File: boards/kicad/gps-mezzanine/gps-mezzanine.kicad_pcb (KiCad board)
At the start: 2 copper layers, 55 x 54 mm, 17 parts, among them J1 CONN_01X04, P1 CONN_02X20, U1 MCP1700T-3302E/TT, U2 FGPMMOPA6H, U3 TXS0104E

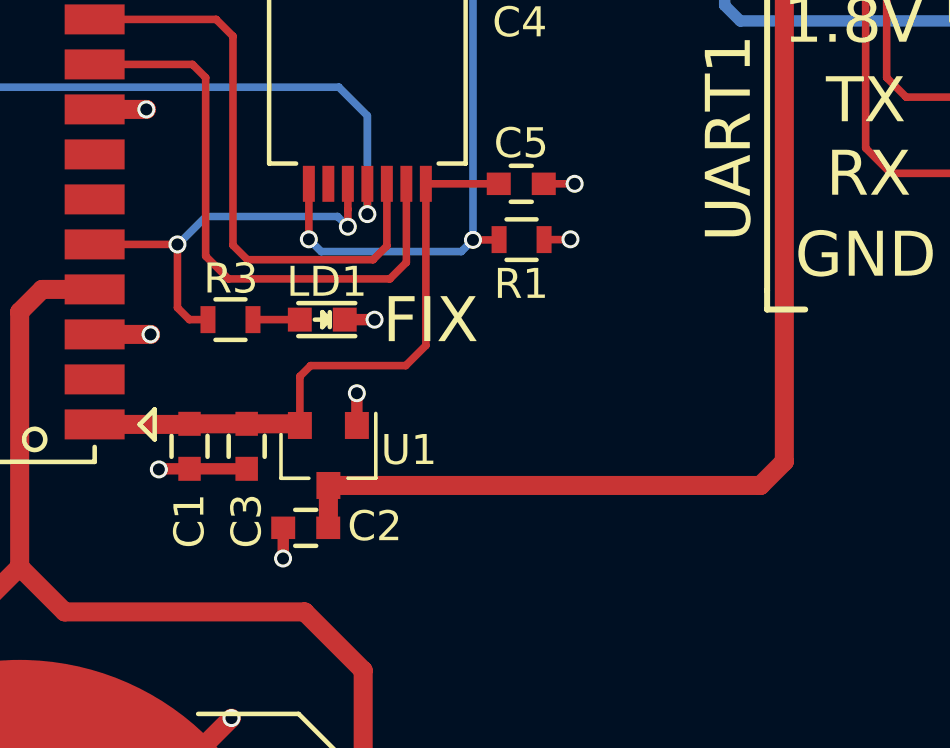
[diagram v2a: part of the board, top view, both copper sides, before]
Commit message: Add ferrite bead to GPS power supply
Signed-off-by: Michael Welling <mwelling@ieee.org>
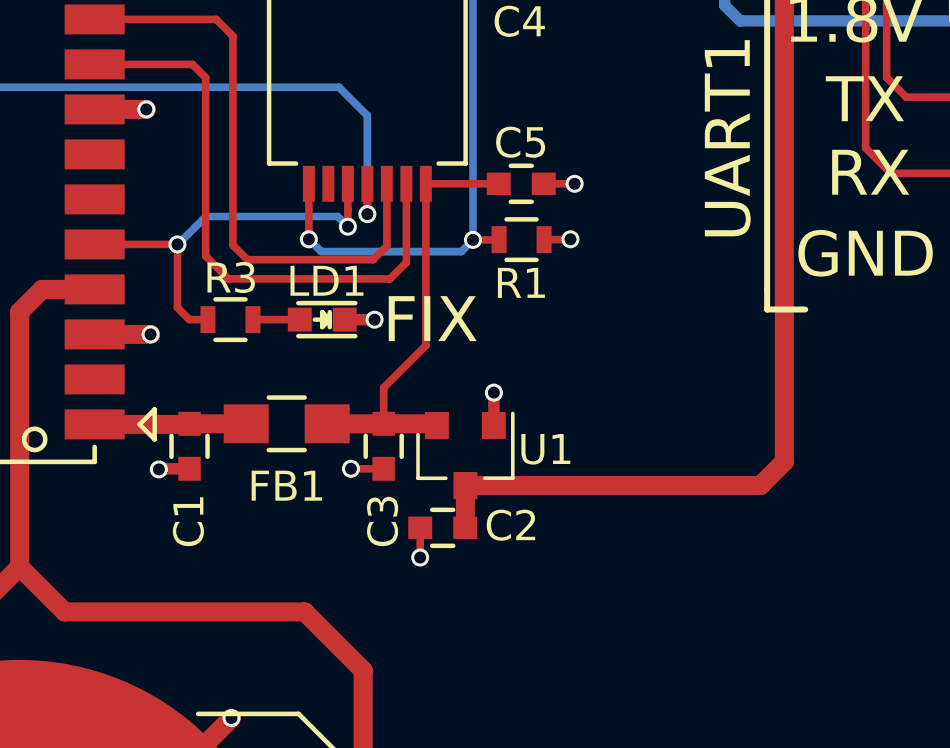
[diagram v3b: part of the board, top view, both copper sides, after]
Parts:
- added FB1: ILBB0805ER102V, Resistors_SMD:R_0805_HandSoldering, F.Cu at (129.4, 125.7)
- moved C2 4.57 mm to (134.6, 129.2)
- moved C3 4.57 mm to (132.6, 126.5)
- moved U1 4.57 mm to (135.4, 126.8)
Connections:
- C1 pad 1: +3V3 -> Net-(C1-Pad1)
- U2 pad 1: +3V3 -> Net-(C1-Pad1)
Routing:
- net +3V3: track 21.0 -> 14.7 mm
- net Net-(C1-Pad1): track 0.00 -> 5.06 mm
- net +5V: track 37.7 -> 33.1 mm
- net GND: track 70.5 -> 69.6 mm, vias 16 -> 17
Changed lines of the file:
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@@
     (thickness 1.6)
     (drawings 23)
-    (tracks 186)
+    (tracks 187)
     (zones 0)
-    (modules 17)
-    (nets 56)
+    (modules 18)
+    (nets 57)
   )
   (page A4)
@@
   (net 54 GPS_1PPS)
   (net 55 "Net-(JK1-Pad1)")
+  (net 56 "Net-(C1-Pad1)")
   (net_class Default "This is the default net class."
     (clearance 0)
@@
     (add_net I2C1_SCL)
     (add_net I2C1_SDA)
+    (add_net "Net-(C1-Pad1)")
     (add_net "Net-(JK1-Pad1)")
     (add_net "Net-(LD1-Pad2)")
@@
     (add_net GND)
   )
+  (module Resistors_SMD:R_0805_HandSoldering (layer F.Cu)
+    (at 129.40156 125.73 180)
+    (descr "Resistor SMD 0805, hand soldering")
+    (tags "resistor 0805")
+    (attr smd)
+    (fp_text reference FB1 (at 0 -2.1 180) (layer F.SilkS)
+      (effects (font (size 1 1) (thickness 0.15)))
+    )
+    (fp_text value ILBB0805ER102V (at -0.00128 1.778 180) (layer F.Fab) hide
+      (effects (font (size 1 1) (thickness 0.15)))
+    )
+    (fp_line (start -2.4 -1) (end 2.4 -1) (layer F.CrtYd) (width 0.05))
+    (fp_line (start -2.4 1) (end 2.4 1) (layer F.CrtYd) (width 0.05))
+    (fp_line (start -2.4 -1) (end -2.4 1) (layer F.CrtYd) (width 0.05))
+    (fp_line (start 2.4 -1) (end 2.4 1) (layer F.CrtYd) (width 0.05))
+    (fp_line (start 0.6 0.875) (end -0.6 0.875) (layer F.SilkS) (width 0.15))
+    (fp_line (start -0.6 -0.875) (end 0.6 -0.875) (layer F.SilkS) (width 0.15))
+    (pad 1 smd rect (at -1.35 0 180) (size 1.5 1.3) (layers F.Cu F.Paste F.Mask)
+      (net 39 +3V3))
+    (pad 2 smd rect (at 1.35 0 180) (size 1.5 1.3) (layers F.Cu F.Paste F.Mask)
+      (net 56 "Net-(C1-Pad1)"))
+    (model Resistors_SMD.3dshapes/R_0805_HandSoldering.wrl
+      (at (xyz 0 0 0))
+      (scale (xyz 1 1 1))
+      (rotate (xyz 0 0 0))
+    )
+  )
   (module Pin_Headers:Pin_Header_Straight_1x04 (layer F.Cu)
     (at 153.1 112.3)
@@
       (effects (font (size 1 1) (thickness 0.15)))
     )
-    (fp_text value TXS0104E (at 0 4.2 270) (layer F.Fab)
+    (fp_text value TXS0104E (at 0 4.2 270) (layer F.Fab) hide
       (effects (font (size 1 1) (thickness 0.15)))
     )
@@
       (effects (font (size 1 1) (thickness 0.15)))
     )
-    (fp_text value .1uF (at 0 -1.42) (layer F.Fab)
+    (fp_text value .1uF (at 0 -1.42) (layer F.Fab) hide
       (effects (font (size 1 1) (thickness 0.15)))
     )
@@
       (effects (font (size 1 1) (thickness 0.15)))
     )
-    (fp_text value .1uF (at -0.09 1.52) (layer F.Fab)
+    (fp_text value .1uF (at -0.09 1.52) (layer F.Fab) hide
       (effects (font (size 1 1) (thickness 0.15)))
     )
@@
       (effects (font (size 1 1) (thickness 0.15)))
     )
-    (fp_text value Battery_Cell (at 0.1 -9.9) (layer F.Fab)
+    (fp_text value Battery_Cell (at 0.1 -9.9) (layer F.Fab) hide
       (effects (font (size 1 1) (thickness 0.15)))
     )
@@
     (fp_line (start -9.5 -6.75) (end -10 -7.25) (layer F.SilkS) (width 0.1524))
     (pad 1 smd rect (at -8 -6.75 180) (size 2 1) (layers F.Cu F.Paste F.Mask)
-      (net 39 +3V3))
+      (net 56 "Net-(C1-Pad1)"))
     (pad 2 smd rect (at -8 -5.25 180) (size 2 1) (layers F.Cu F.Paste F.Mask)
       (net 42 "Net-(U2-Pad2)"))
@@
   )
   (module Capacitors_SMD:C_0603 (layer F.Cu)
-    (at 128.067 126.48 270)
+    (at 132.63392 126.48 270)
     (descr "Capacitor SMD 0603, reflow soldering, AVX (see smccp.pdf)")
     (tags "capacitor 0603")
@@
   )
   (module Capacitors_SMD:C_0603 (layer F.Cu)
-    (at 130.0353 129.1971 180)
+    (at 134.60222 129.1971 180)
     (descr "Capacitor SMD 0603, reflow soldering, AVX (see smccp.pdf)")
     (tags "capacitor 0603")
@@
     (fp_line (start 0.35 0.6) (end -0.35 0.6) (layer F.SilkS) (width 0.15))
     (pad 1 smd rect (at -0.75 0 270) (size 0.8 0.75) (layers F.Cu F.Paste F.Mask)
-      (net 39 +3V3))
+      (net 56 "Net-(C1-Pad1)"))
     (pad 2 smd rect (at 0.75 0 270) (size 0.8 0.75) (layers F.Cu F.Paste F.Mask)
       (net 2 GND))
@@
   )
   (module TO_SOT_Packages_SMD:SOT-23 (layer F.Cu)
-    (at 130.790995 126.785215 270)
+    (at 135.357915 126.785215 270)
     (descr "SOT-23, Standard")
     (tags SOT-23)
@@
   (segment (start 144 106.25) (end 144 109) (width 0.635) (layer B.Cu) (net 1))
   (via (at 144 109) (size 0.6) (drill 0.4) (layers F.Cu B.Cu) (net 1))
+  (segment (start 133.85222 129.1971) (end 133.85222 130.18586) (width 0.254) (layer F.Cu) (net 2))
+  (segment (start 133.85222 130.18586) (end 133.85038 130.1877) (width 0.254) (layer F.Cu) (net 2))
+  (via (at 133.85038 130.1877) (size 0.6) (drill 0.4) (layers F.Cu B.Cu) (net 2))
+  (segment (start 132.63392 127.23) (end 131.54546 127.23) (width 0.254) (layer F.Cu) (net 2))
+  (segment (start 131.54546 127.23) (end 131.54406 127.2286) (width 0.254) (layer F.Cu) (net 2))
+  (via (at 131.54406 127.2286) (size 0.6) (drill 0.4) (layers F.Cu B.Cu) (net 2))
+  (via (at 136.307915 124.690675) (size 0.6) (drill 0.4) (layers F.Cu B.Cu) (net 2))
   (segment (start 120.55 142.46) (end 113.55 135.46) (width 0.635) (layer F.Cu) (net 2))
   (via (at 113.55 135.46) (size 0.6) (drill 0.4) (layers F.Cu B.Cu) (net 2))
@@
   (segment (start 107 124.25) (end 105.34 124.25) (width 0.635) (layer F.Cu) (net 2))
   (via (at 105.34 124.25) (size 0.6) (drill 0.4) (layers F.Cu B.Cu) (net 2))
-  (segment (start 129.2853 129.1971) (end 129.2853 130.2147) (width 0.381) (layer F.Cu) (net 2))
-  (segment (start 129.2853 130.2147) (end 129.28 130.22) (width 0.381) (layer F.Cu) (net 2))
-  (via (at 129.28 130.22) (size 0.6) (drill 0.4) (layers F.Cu B.Cu) (net 2))
   (segment (start 126.162 127.23) (end 125.16 127.23) (width 0.381) (layer F.Cu) (net 2))
   (segment (start 125.16 127.23) (end 125.14 127.25) (width 0.381) (layer F.Cu) (net 2))
   (via (at 125.14 127.25) (size 0.6) (drill 0.4) (layers F.Cu B.Cu) (net 2))
-  (segment (start 128.067 127.23) (end 126.162 127.23) (width 0.381) (layer F.Cu) (net 2))
-  (segment (start 131.740995 125.785215) (end 131.740995 124.710995) (width 0.381) (layer F.Cu) (net 2))
-  (segment (start 131.740995 124.710995) (end 131.74 124.71) (width 0.381) (layer F.Cu) (net 2))
-  (via (at 131.74 124.71) (size 0.6) (drill 0.4) (layers F.Cu B.Cu) (net 2))
+  (segment (start 136.307915 125.764895) (end 136.307915 124.690675) (width 0.381) (layer F.Cu) (net 2))
+  (segment (start 136.307915 124.690675) (end 136.30692 124.68968) (width 0.381) (layer F.Cu) (net 2))
   (segment (start 131.337 122.257) (end 132.327 122.257) (width 0.381) (layer F.Cu) (net 2))
   (segment (start 132.327 122.257) (end 132.33 122.26) (width 0.381) (layer F.Cu) (net 2))
@@
   (segment (start 105.36292 113.75) (end 105.36174 113.74882) (width 0.635) (layer F.Cu) (net 2))
   (via (at 105.36174 113.74882) (size 0.6) (drill 0.4) (layers F.Cu B.Cu) (net 2))
-  (segment (start 145.194785 127.785215) (end 130.790995 127.785215) (width 0.635) (layer F.Cu) (net 3))
+  (segment (start 145.194785 127.785215) (end 135.357915 127.785215) (width 0.635) (layer F.Cu) (net 3))
   (segment (start 145.194785 127.785215) (end 145.98904 126.99096) (width 0.635) (layer F.Cu) (net 3))
   (segment (start 145.98904 126.99096) (end 145.98904 108.91266) (width 0.635) (layer F.Cu) (net 3))
-  (segment (start 130.790995 127.785215) (end 130.790995 129.191405) (width 0.635) (layer F.Cu) (net 3))
-  (segment (start 130.790995 129.191405) (end 130.7853 129.1971) (width 0.635) (layer F.Cu) (net 3))
+  (segment (start 135.357915 127.785215) (end 135.357915 129.191405) (width 0.635) (layer F.Cu) (net 3))
+  (segment (start 135.357915 129.191405) (end 135.35222 129.1971) (width 0.635) (layer F.Cu) (net 3))
   (segment (start 145.98904 108.91266) (end 145.98904 106.26096) (width 0.635) (layer B.Cu) (net 3))
   (segment (start 145.98904 106.26096) (end 146 106.25) (width 0.635) (layer B.Cu) (net 3))
@@
   (segment (start 132.74 119.8) (end 132.74 117.73) (width 0.254) (layer F.Cu) (net 38))
   (segment (start 123.085 112.335) (end 123 112.25) (width 0.254) (layer F.Cu) (net 38))
-  (segment (start 133.37 123.79) (end 134.04 123.12) (width 0.254) (layer F.Cu) (net 39))
-  (segment (start 134.04 123.12) (end 134.04 117.73) (width 0.254) (layer F.Cu) (net 39))
-  (segment (start 130.2 123.79) (end 133.37 123.79) (width 0.254) (layer F.Cu) (net 39))
-  (segment (start 129.840995 124.149005) (end 130.2 123.79) (width 0.254) (layer F.Cu) (net 39))
-  (segment (start 129.840995 125.785215) (end 129.840995 124.149005) (width 0.254) (layer F.Cu) (net 39))
+  (segment (start 134.04 117.73) (end 134.04 123.12) (width 0.254) (layer F.Cu) (net 39))
+  (segment (start 134.04 123.12) (end 132.63392 124.52608) (width 0.254) (layer F.Cu) (net 39))
+  (segment (start 132.63392 124.52608) (end 132.63392 125.73) (width 0.254) (layer F.Cu) (net 39))
+  (segment (start 130.75156 125.73) (end 132.63392 125.73) (width 0.635) (layer F.Cu) (net 39))
   (segment (start 136.47 117.73) (end 134.04 117.73) (width 0.254) (layer F.Cu) (net 39))
-  (segment (start 128.067 125.73) (end 129.78578 125.73) (width 0.635) (layer F.Cu) (net 39))
-  (segment (start 129.78578 125.73) (end 129.840995 125.785215) (width 0.635) (layer F.Cu) (net 39))
-  (segment (start 126.162 125.73) (end 128.067 125.73) (width 0.635) (layer F.Cu) (net 39))
-  (segment (start 123 125.75) (end 126.142 125.75) (width 0.635) (layer F.Cu) (net 39))
-  (segment (start 126.142 125.75) (end 126.162 125.73) (width 0.635) (layer F.Cu) (net 39))
+  (segment (start 132.63392 125.73) (end 134.3527 125.73) (width 0.635) (layer F.Cu) (net 39))
+  (segment (start 134.3527 125.73) (end 134.407915 125.785215) (width 0.635) (layer F.Cu) (net 39))
+  (segment (start 126.162 125.73) (end 128.05156 125.73) (width 0.635) (layer F.Cu) (net 56))
+  (segment (start 123 125.75) (end 126.142 125.75) (width 0.635) (layer F.Cu) (net 56))
+  (segment (start 126.142 125.75) (end 126.162 125.73) (width 0.635) (layer F.Cu) (net 56))
   (segment (start 128.277 122.257) (end 129.8384 122.257) (width 0.254) (layer F.Cu) (net 40))
   (segment (start 131.44 119.16) (end 131.1 118.82) (width 0.254) (layer B.Cu) (net 41))
